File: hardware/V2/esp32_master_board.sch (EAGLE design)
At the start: 62 parts, among them IC1 SN74HC138PW, IC2 MAX17502EATB+T, SW1 B3U-1000P-2P-SMD

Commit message: [HARDWARE] Continue V2 design
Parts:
- added IC3, IC4: WS2812B, WS2812B:WS2812B
- added U$5: DF13-3P-1.25DSA, con-hirose-df13:DF13-3P-1.25DSA
- added U$6: DF13-4P-1.25DSA, con-hirose-df13:DF13-4P-1.25DSA
- C10: device resistor:C-EUC0805K -> resistor:C-EUC1210
- C17: value 1u -> 22u
- U$4: value DF13-7P-1.25DSA -> DF13-6P-1.25DSA; device con-hirose-df13:DF13-7P-1.25DSA -> con-hirose-df13:DF13-6P-1.25DSA
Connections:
- removed net I35: U$1.GPIO35, U$4.3
- removed net IO32: U$1.GPIO32, U$4.5
- new net I35_RX1: U$1.GPIO35, U$6.2
- new net IO32_TX1: U$1.GPIO32, U$6.3
- new net N$19: IC3.DOUT, IC4.DIN
- new net WSLED_OUT: IC4.DOUT, U$5.3
- net 5V: now also IC3.VDD, IC4.VDD, U$4.5, U$5.2, U$6.4
- net GND: now also IC3.VSS, IC4.VSS, U$5.1, U$6.1
- net IO2: now also IC3.DIN, U$4.3; no longer U$4.4
- net IO33: now also U$4.4; no longer U$4.6
- net VCC: now also U$4.6; no longer U$4.7

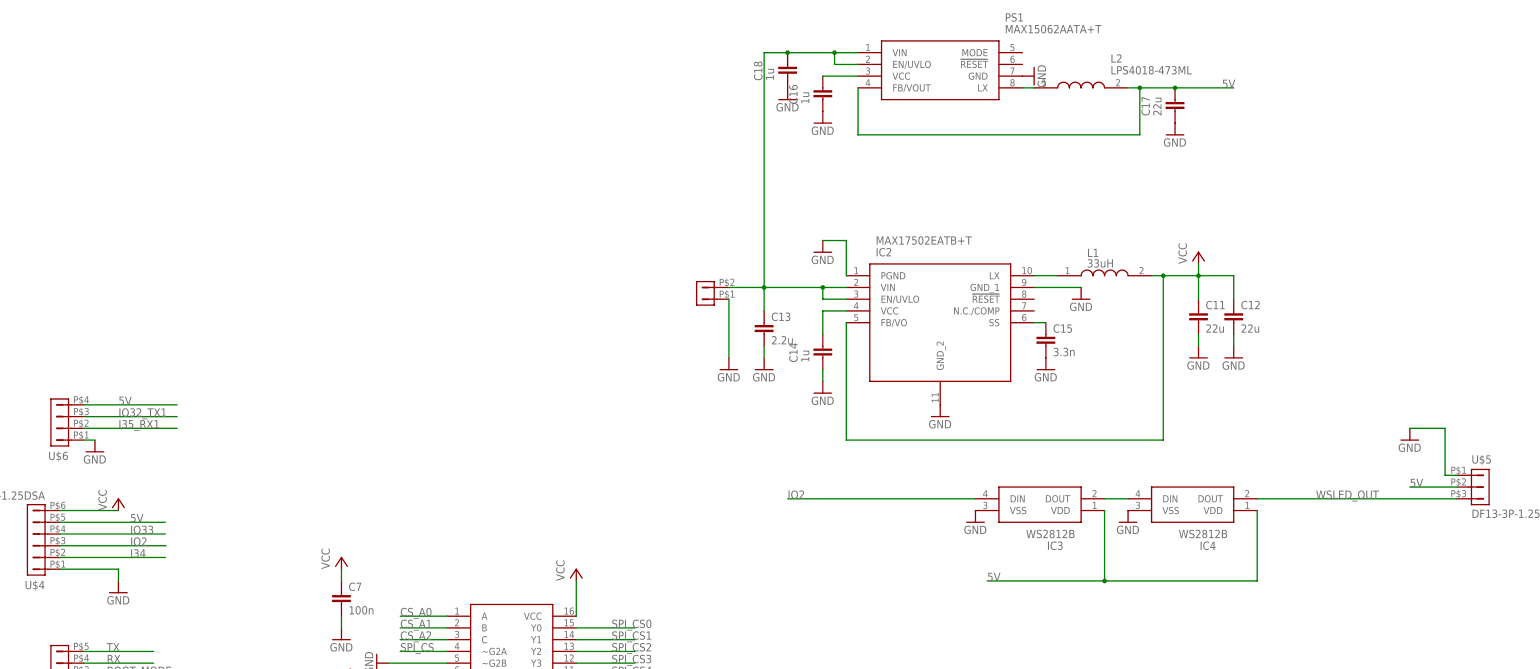
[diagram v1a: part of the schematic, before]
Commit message: [HARDWARE] simplify design of the V2 removing the 5V since IMU is ok with 3.3V. WS2812 LEDs are out of spec for 3.3V but works in practice. The LED are not critical, and 5V LED would require a level shifter
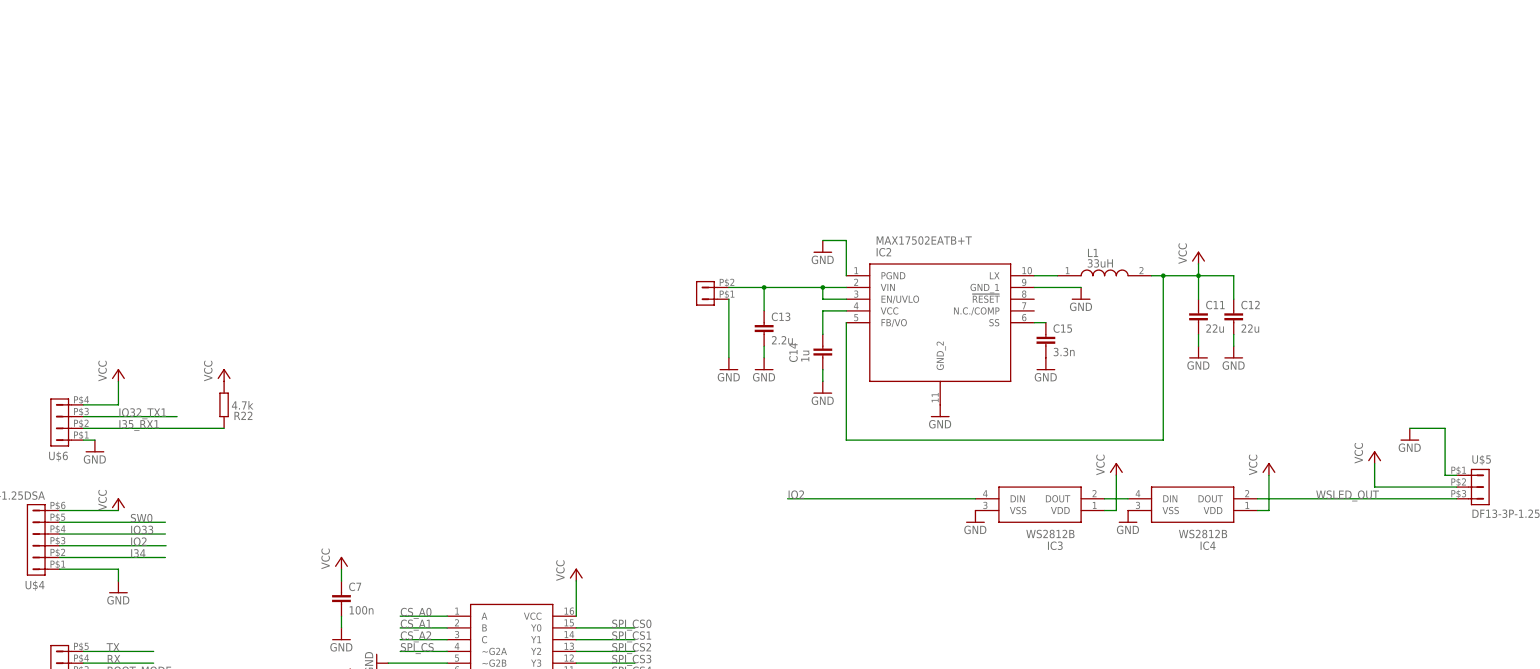
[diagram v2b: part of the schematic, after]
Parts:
- removed C16, C18: 1u, resistor:C-EUC0402
- removed C17: 22u, resistor:C-EUC1210
- removed L2: LPS4018-473ML, LPS4018-333MRC:LPS4018-333MRC
- removed PS1: MAX15062AATA+T, MAX15062AATA:MAX15062AATA+T
- added R22: 4.7k, resistor:R-EU_R0402
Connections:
- removed net 5V: C17.2, IC3.VDD, IC4.VDD, L2.2, PS1.FB/VOUT, U$4.5, U$5.2, U$6.4
- removed net N$22: L2.1, PS1.LX
- removed net N$24: C16.2, PS1.VCC
- net GND: no longer C16.1, C17.1, C18.1, PS1.GND
- net I35_RX1: now also R22.2
- net N$25: no longer C18.2, PS1.EN/UVLO, PS1.VIN
- net SW0: now also U$4.5
- net VCC: now also IC3.VDD, IC4.VDD, R22.1, U$5.2, U$6.4

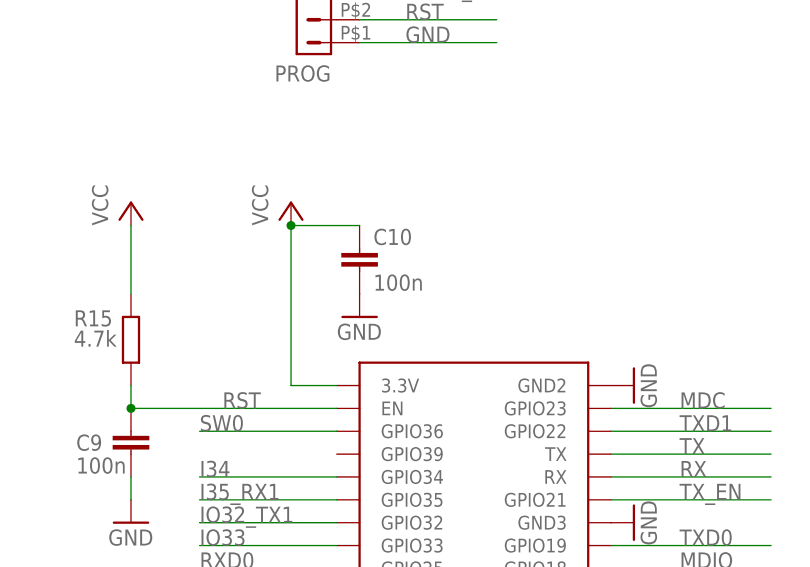
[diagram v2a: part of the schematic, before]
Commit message: [hardware] increase clearance around the holes, minor changes
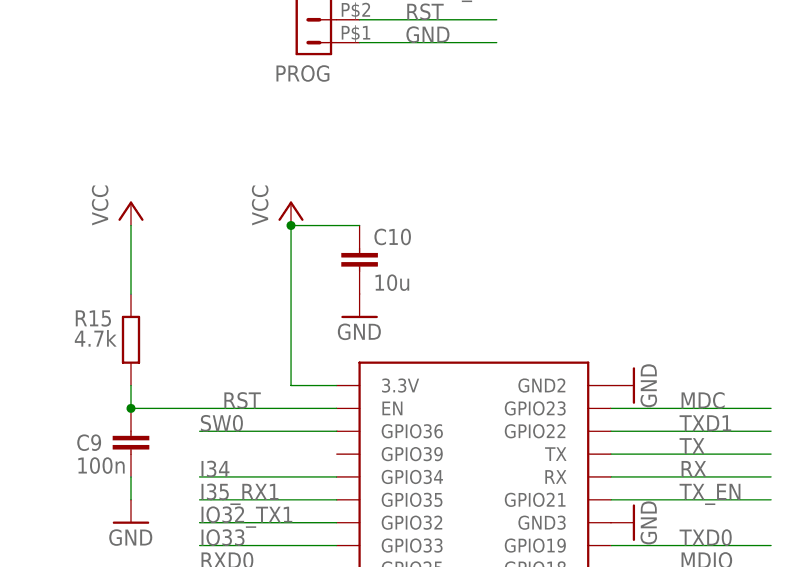
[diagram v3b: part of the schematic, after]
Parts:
- C10: value 100n -> 10u
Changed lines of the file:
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@@
 <part name="C9" library="resistor" library_urn="urn:adsk.eagle:library:348" deviceset="C-EU" device="C0402" package3d_urn="urn:adsk.eagle:package:23626/2" value="100n"/>
 <part name="PROG" library="con-hirose-df13" deviceset="DF13-5P-1.25" device="DSA"/>
-<part name="C10" library="resistor" library_urn="urn:adsk.eagle:library:348" deviceset="C-EU" device="C1210" package3d_urn="urn:adsk.eagle:package:23619/2" value="100n"/>
+<part name="C10" library="resistor" library_urn="urn:adsk.eagle:library:348" deviceset="C-EU" device="C1210" package3d_urn="urn:adsk.eagle:package:23619/2" value="10u"/>
 <part name="GND24" library="supply1" library_urn="urn:adsk.eagle:library:371" deviceset="GND" device=""/>
 <part name="R16" library="resistor" library_urn="urn:adsk.eagle:library:348" deviceset="R-EU_" device="R0402" package3d_urn="urn:adsk.eagle:package:26058/2" value="4.7k"/>

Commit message: [hardware] V2.1: Add MPN for all parts, fix some footprints, add BOM compatible with seeedfusion PCBA, add pick and place files
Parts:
- C1: MANUFACTURER_PART_NUMBER (none) -> 885012205052
- C10: value 10u -> 22u; device resistor:C-EUC1210 -> rcl:C-EUC0805; MANUFACTURER_PART_NUMBER (none) -> CPL-CAP-X5R-0805-22UF-6.3V
- C11, C12: device resistor:C-EUC1210 -> rcl:C-EUC0805; MANUFACTURER_PART_NUMBER (none) -> CPL-CAP-X5R-0805-22UF-6.3V
- C13: MANUFACTURER_PART_NUMBER (none) -> C3225X7R1H225K250AB
- C14, C3: MANUFACTURER_PART_NUMBER (none) -> CPL-CAP-X5R-0402-1UF-6.3V
- C15: MANUFACTURER_PART_NUMBER (none) -> 885012205064
- C2: MANUFACTURER_PART_NUMBER (none) -> 0101ZC471KAT2A
- C4, C5, C6, C7, C8, C9: MANUFACTURER_PART_NUMBER (none) -> CPL-CAP-X7R-0402-100NF-16V
- D1: device led:LEDCHIPLED_0805 -> led:LEDCHIPLED_0603; MANUFACTURER_PART_NUMBER (none) -> CPL-LED-0603-RED
- D2: device led:LEDCHIPLED_0805 -> led:LEDCHIPLED_0603; MANUFACTURER_PART_NUMBER (none) -> CPL-LED-0603-GREEN
- L: value (none) -> 0; MANUFACTURER_PART_NUMBER (none) -> CPL-RES-0402-0-0.063W
- L1: value 33uH -> 15uH; device LPS6235-682MRB:LPS6235-682MRB -> LPS6235-153MRB:LPS6235-153MRB
- POWER, U$5: MANUFACTURER_PART_NUMBER (none) -> DF13-3P-1.25DSA
- PROG, SPI_0, SPI_1, SPI_2, SPI_3, SPI_4, SPI_5, SPI_6, SPI_7: MANUFACTURER_PART_NUMBER (none) -> DF13-5P-1.25DSA
- R1, R2, R20, R21, R3, R4: MANUFACTURER_PART_NUMBER (none) -> CPL-RES-0402-10-0.063W
- R10, R11, R12, R13: MANUFACTURER_PART_NUMBER (none) -> CRCW040249R9FKEDC
- R14, R18, R8, R9: MANUFACTURER_PART_NUMBER (none) -> RC0402JR-13330RL
- R15, R16, R19, R22, R5: MANUFACTURER_PART_NUMBER (none) -> CPL-RES-0402-4.7K-0.063W
- R17: MANUFACTURER_PART_NUMBER (none) -> CPL-RES-0603-1.5K-0.1W
- R6: MANUFACTURER_PART_NUMBER (none) -> CRCW040233R0FKEDC
- R7: MANUFACTURER_PART_NUMBER (none) -> ERJ-U02F1212X
- SW1: MANUFACTURER_PART_NUMBER (none) -> B3U-1000P
- U$1: MANUFACTURER_PART_NUMBER (none) -> ESP32-WROOM-32D
- U$2: MANUFACTURER_PART_NUMBER (none) -> LAN8720A-CP
- U$3: MANUFACTURER_PART_NUMBER (none) -> HR911105A
- U$4: MANUFACTURER_PART_NUMBER (none) -> DF13-6P-1.25DSA
- U$6: MANUFACTURER_PART_NUMBER (none) -> DF13-4P-1.25DSA
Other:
- note added: "MASTER BOARD V2.1 LAAS CNRS - Thomas FLAYOLS https://github.com/open-dynamic-robot-initiative/master-board"
- moved on the sheet: IC3, IC4, PROG, R22, SPI_0, SPI_1, SPI_2, SPI_3, SPI_4, SPI_5, SPI_6, SPI_7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
